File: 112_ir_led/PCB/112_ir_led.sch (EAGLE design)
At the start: 5 parts

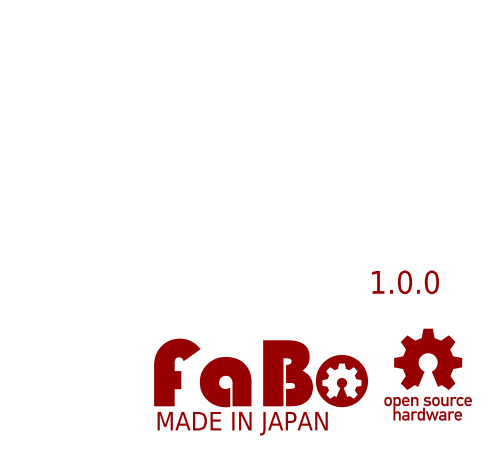
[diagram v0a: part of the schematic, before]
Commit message: add product number
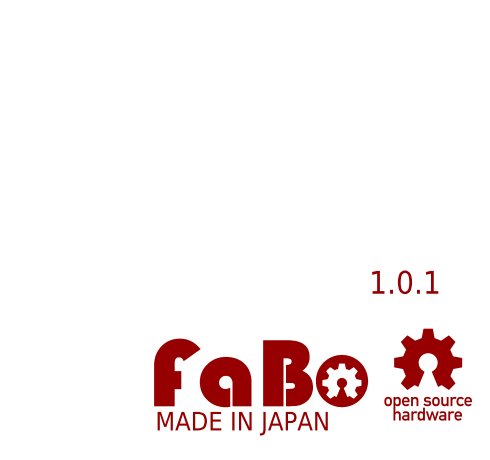
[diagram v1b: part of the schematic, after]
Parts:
- U$3: device FaBo-etc:LOGO_OSHW-T_M -> FaBo-etc:LOGO_OSHW-T_M_BOTTOM
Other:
- note added: "1.0.1"
- note removed: "1.0.0"
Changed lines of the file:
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@@
 <part name="U$1" library="FaBo-etc" deviceset="A4L-LOC" device=""/>
 <part name="U$2" library="FaBo-etc" deviceset="LOGO_FABO" device="-M"/>
-<part name="U$3" library="FaBo-etc" deviceset="LOGO_OSHW" device="-T_M"/>
+<part name="U$3" library="FaBo-etc" deviceset="LOGO_OSHW" device="-T_M_BOTTOM"/>
 </parts>
 <sheets>
 <sheet>
 <plain>
-<text x="246.38" y="20.32" size="2.54" layer="94" align="bottom-center">1.0.0</text>
+<text x="246.38" y="20.32" size="2.54" layer="94" align="bottom-center">1.0.1</text>
 </plain>
 <instances>

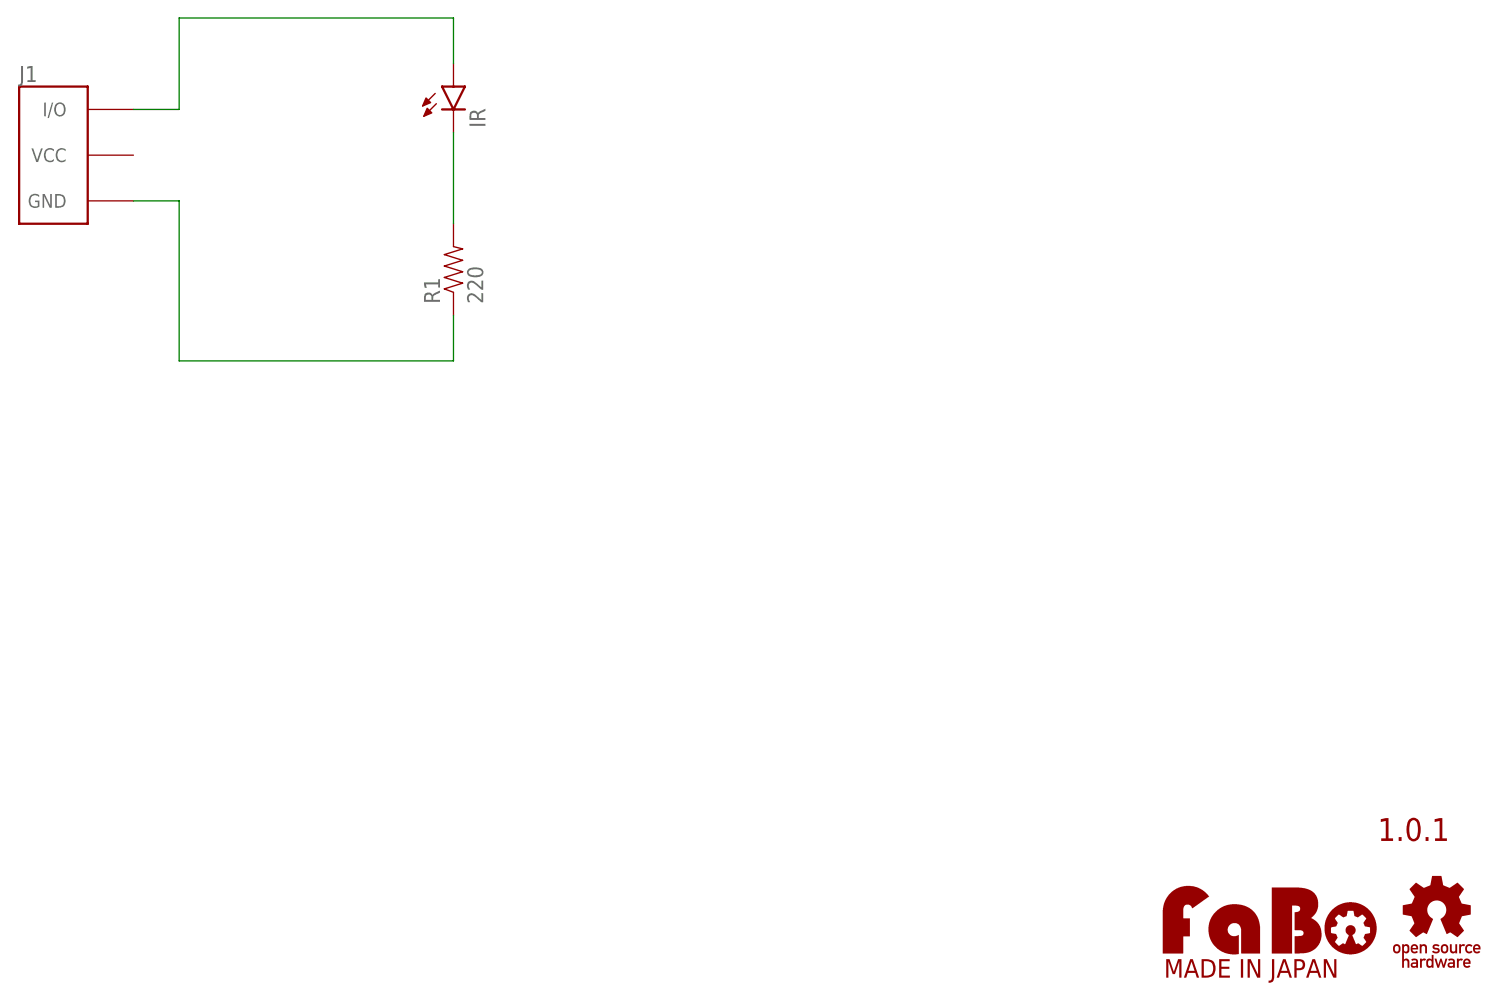
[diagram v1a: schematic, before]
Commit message: fix solder land(non-check)
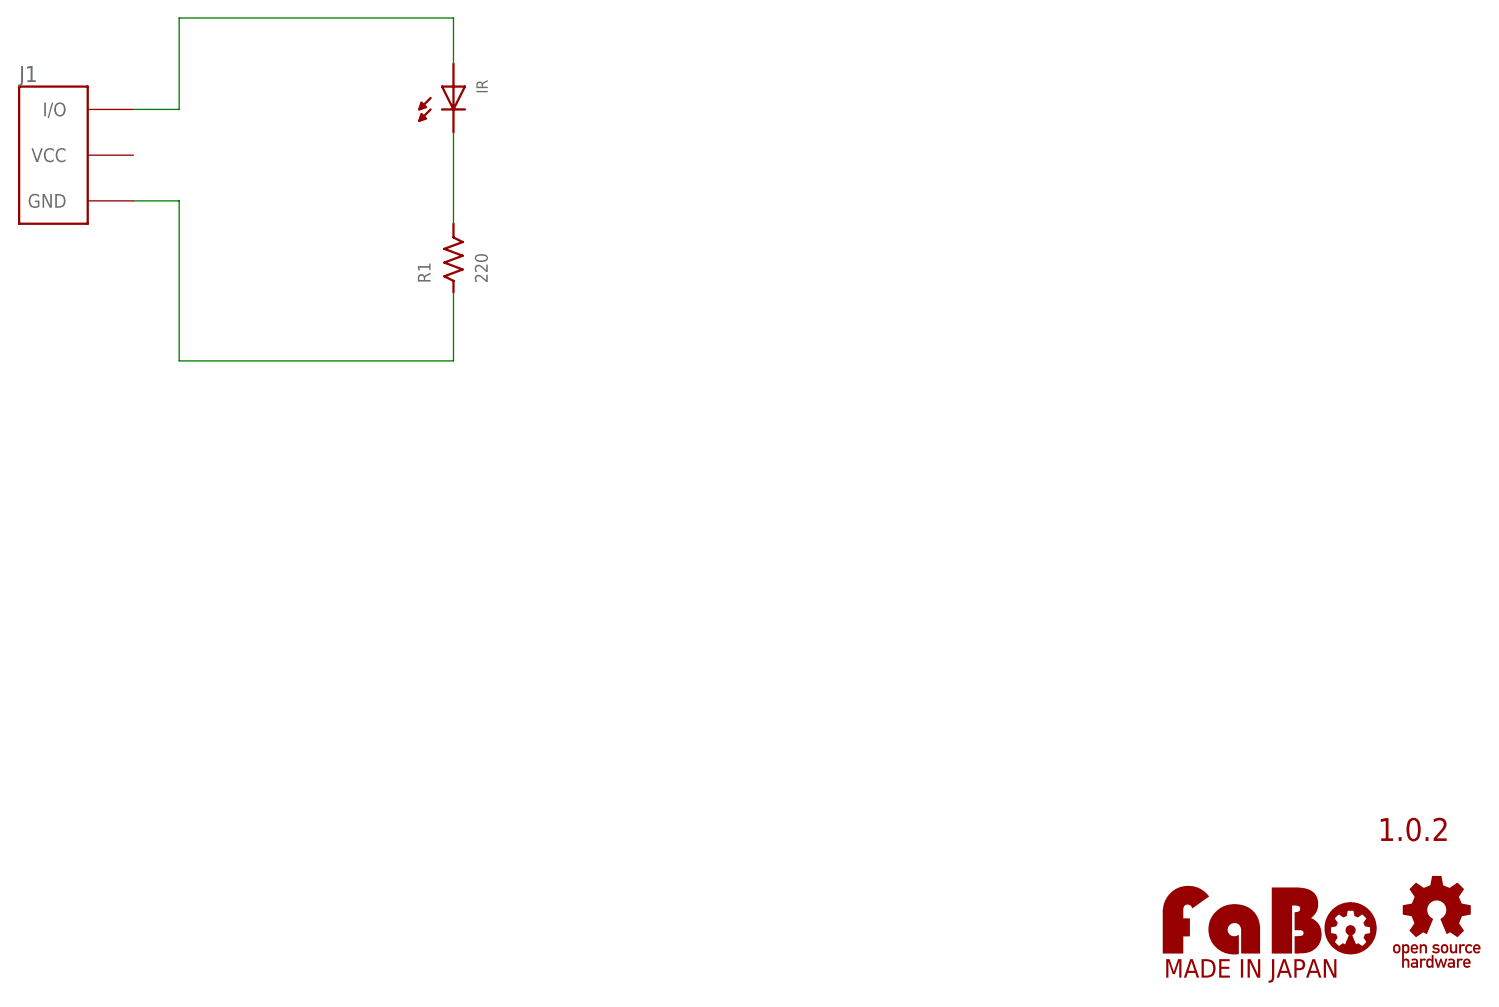
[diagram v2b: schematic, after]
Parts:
- IR: device FaBo-etc:LED-5MM -> FaBo-LED:LED-5MM
- R1: device FaBo-etc:RES-PTH-REGULAR -> FaBo-Resistors:RESISTOR-AXL-REGULAR
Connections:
- net N$1: now also IR.ANODE; no longer IR.A
- net N$2: now also IR.CATHODE; no longer IR.C
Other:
- note added: "1.0.2"
- note removed: "1.0.1"
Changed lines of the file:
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@@
 <?xml version="1.0" encoding="utf-8"?>
 <!DOCTYPE eagle SYSTEM "eagle.dtd">
-<eagle version="7.4.0">
+<eagle version="7.5.0">
 <drawing>
 <settings>
@@
 <parts>
 <part name="J1" library="FaBo-Template" deviceset="FABO_BRICK_3PIN" device=""/>
-<part name="IR" library="FaBo-etc" deviceset="LED" device="-5MM"/>
-<part name="R1" library="FaBo-etc" deviceset="RES" device="-PTH-REGULAR" value="220"/>
 <part name="U$1" library="FaBo-etc" deviceset="A4L-LOC" device=""/>
 <part name="U$2" library="FaBo-etc" deviceset="LOGO_FABO" device="-M"/>
 <part name="U$3" library="FaBo-etc" deviceset="LOGO_OSHW" device="-T_M_BOTTOM"/>
+<part name="IR" library="FaBo-LED" deviceset="LED" device="-5MM"/>
+<part name="R1" library="FaBo-Resistors" deviceset="RESISTOR" device="-AXL-REGULAR" value="220"/>
 </parts>
 <sheets>
 <sheet>
 <plain>
-<text x="246.38" y="20.32" size="2.54" layer="94" align="bottom-center">1.0.1</text>
+<text x="246.38" y="20.32" size="2.54" layer="94" align="bottom-center">1.0.2</text>
 </plain>
 <instances>
 <instance part="J1" gate="G$1" x="96.52" y="96.52"/>
-<instance part="IR" gate="G$1" x="139.7" y="101.6"/>
-<instance part="R1" gate="G$1" x="139.7" y="83.82" rot="R90"/>
 <instance part="U$1" gate="G$1" x="0" y="0"/>
 <instance part="U$2" gate="G$1" x="218.44" y="5.08"/>
 <instance part="U$3" gate="G$1" x="248.92" y="12.7"/>
+<instance part="IR" gate="G$1" x="139.7" y="104.14" rot="R270"/>
+<instance part="R1" gate="G$1" x="139.7" y="83.82" rot="R90"/>
 </instances>
 <busses>
@@
 <wire x1="139.7" y1="111.76" x2="139.7" y2="106.68" width="0.1524" layer="91"/>
 <pinref part="J1" gate="G$1" pin="I/O"/>
-<pinref part="IR" gate="G$1" pin="A"/>
+<pinref part="IR" gate="G$1" pin="ANODE"/>
 </segment>
 </net>
@@
 <segment>
 <wire x1="139.7" y1="99.06" x2="139.7" y2="88.9" width="0.1524" layer="91"/>
-<pinref part="IR" gate="G$1" pin="C"/>
+<pinref part="IR" gate="G$1" pin="CATHODE"/>
 <pinref part="R1" gate="G$1" pin="2"/>
 </segment>
@@
 <wire x1="109.22" y1="91.44" x2="109.22" y2="73.66" width="0.1524" layer="91"/>
 <wire x1="109.22" y1="73.66" x2="139.7" y2="73.66" width="0.1524" layer="91"/>
-<wire x1="139.7" y1="73.66" x2="139.7" y2="78.74" width="0.1524" layer="91"/>
+<wire x1="139.7" y1="73.66" x2="139.7" y2="81.28" width="0.1524" layer="91"/>
 <pinref part="J1" gate="G$1" pin="GND"/>
 <pinref part="R1" gate="G$1" pin="1"/>

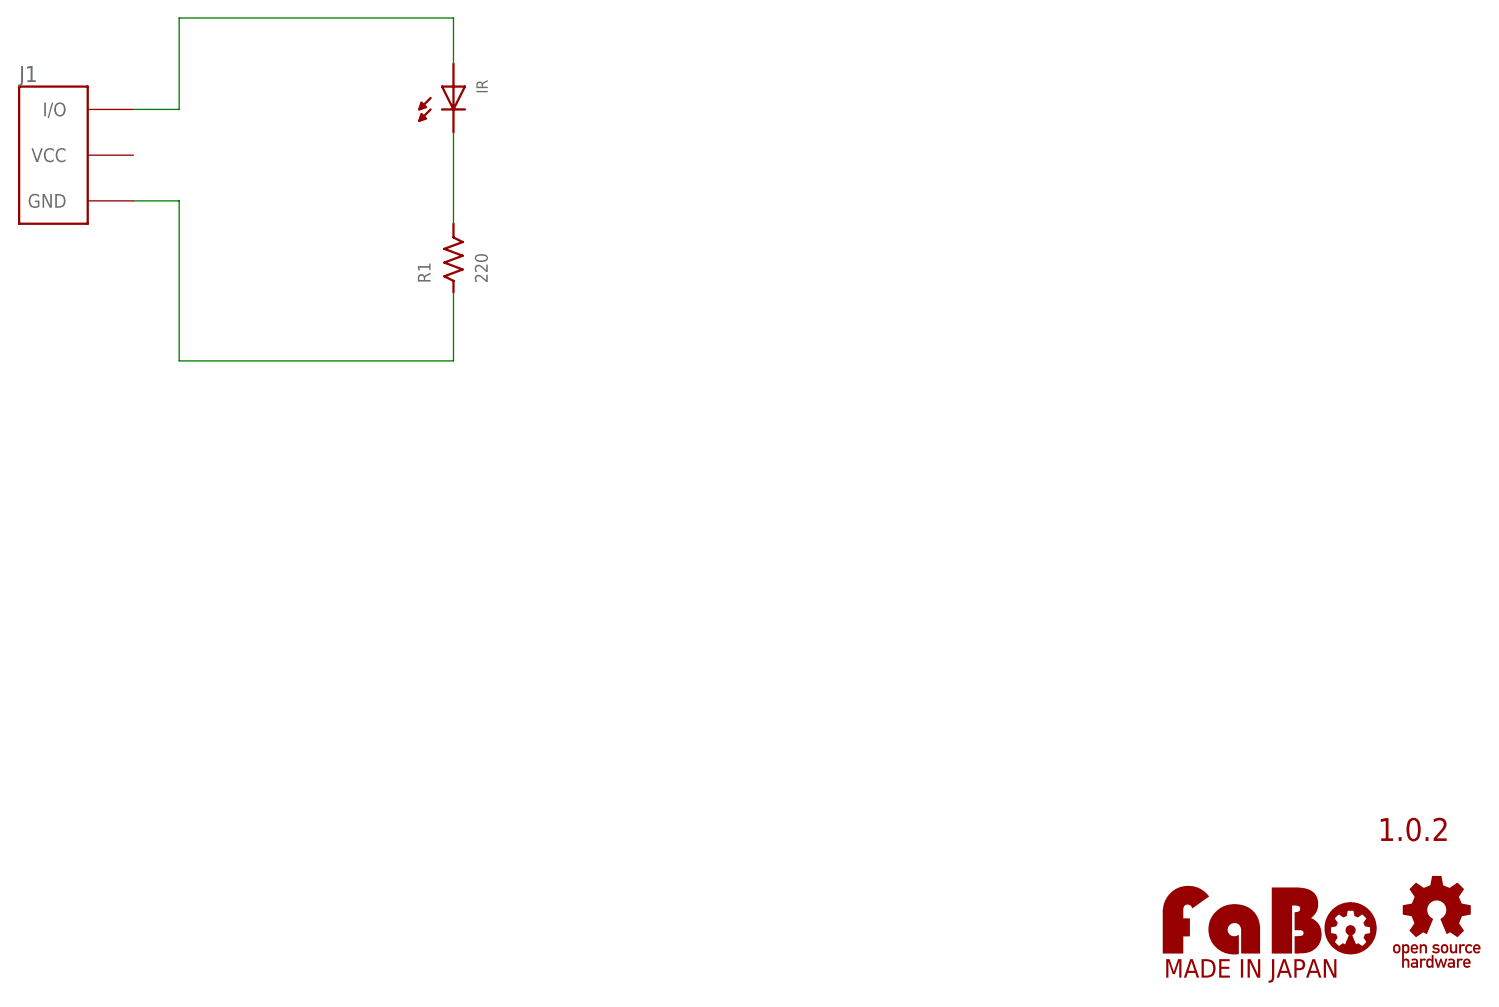
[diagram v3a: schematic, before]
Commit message: change jst connector
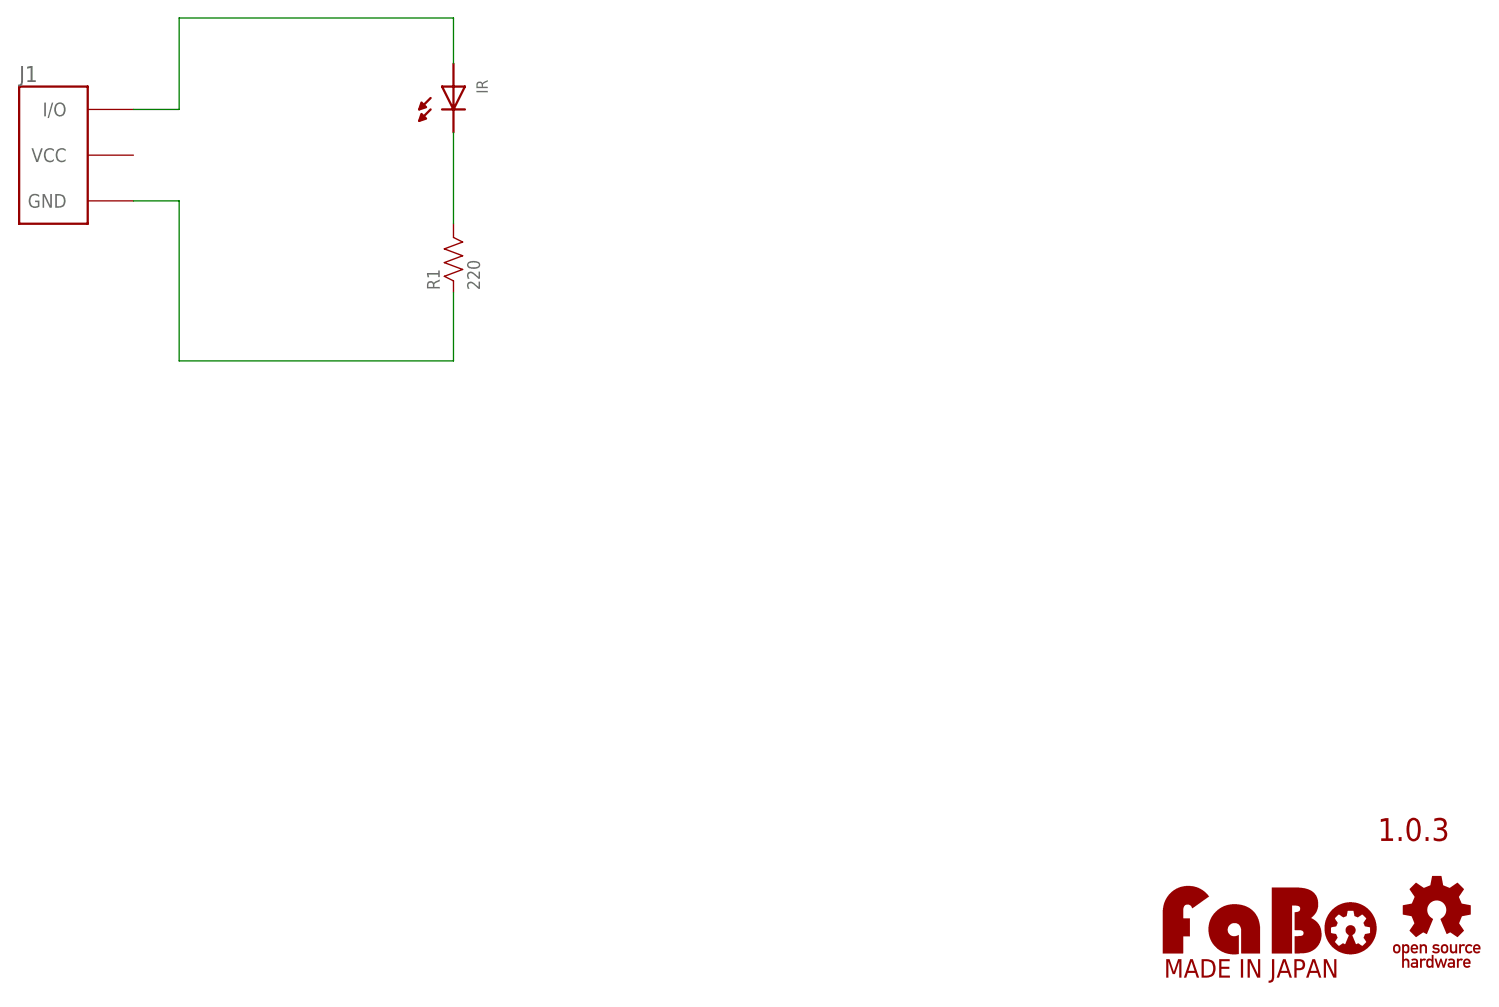
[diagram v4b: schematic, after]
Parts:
- U$3: device FaBo-etc:LOGO_OSHW-T_M_BOTTOM -> FaBo-etc:LOGO_OSHW-M_BOTTOM
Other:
- note added: "1.0.3"
- note removed: "1.0.2"
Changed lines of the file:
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@@
 <?xml version="1.0" encoding="utf-8"?>
 <!DOCTYPE eagle SYSTEM "eagle.dtd">
-<eagle version="7.5.0">
+<eagle version="7.6.0">
 <drawing>
 <settings>
@@
 <part name="U$1" library="FaBo-etc" deviceset="A4L-LOC" device=""/>
 <part name="U$2" library="FaBo-etc" deviceset="LOGO_FABO" device="-M"/>
-<part name="U$3" library="FaBo-etc" deviceset="LOGO_OSHW" device="-T_M_BOTTOM"/>
 <part name="IR" library="FaBo-LED" deviceset="LED" device="-5MM"/>
 <part name="R1" library="FaBo-Resistors" deviceset="RESISTOR" device="-AXL-REGULAR" value="220"/>
+<part name="U$3" library="FaBo-etc" deviceset="LOGO_OSHW" device="-M_BOTTOM"/>
 </parts>
 <sheets>
 <sheet>
 <plain>
-<text x="246.38" y="20.32" size="2.54" layer="94" align="bottom-center">1.0.2</text>
+<text x="246.38" y="20.32" size="2.54" layer="94" align="bottom-center">1.0.3</text>
 </plain>
 <instances>
@@
 <instance part="U$1" gate="G$1" x="0" y="0"/>
 <instance part="U$2" gate="G$1" x="218.44" y="5.08"/>
-<instance part="U$3" gate="G$1" x="248.92" y="12.7"/>
 <instance part="IR" gate="G$1" x="139.7" y="104.14" rot="R270"/>
 <instance part="R1" gate="G$1" x="139.7" y="83.82" rot="R90"/>
+<instance part="U$3" gate="G$1" x="248.92" y="12.7"/>
 </instances>
 <busses>
